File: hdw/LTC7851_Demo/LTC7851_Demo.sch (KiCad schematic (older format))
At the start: 0 parts

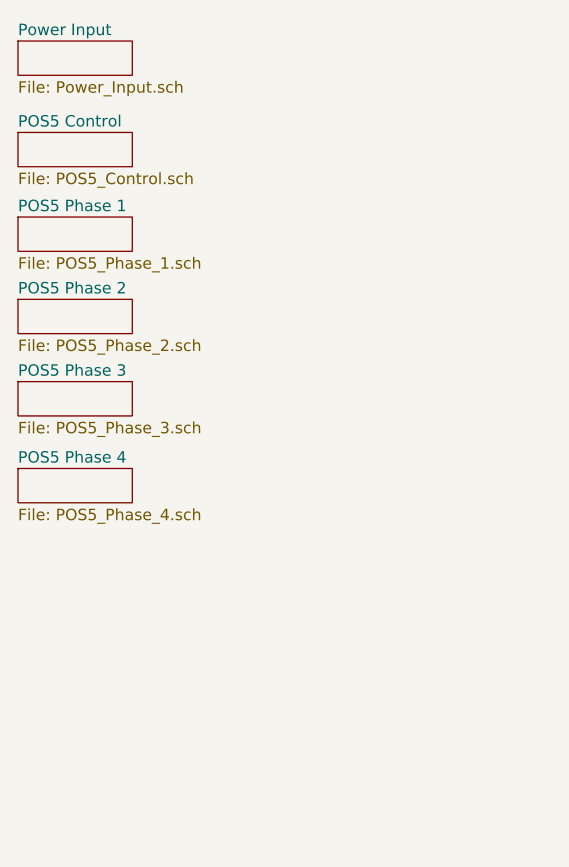
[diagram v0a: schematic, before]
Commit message: Added LDO for VCC input, cleaned some stuff up
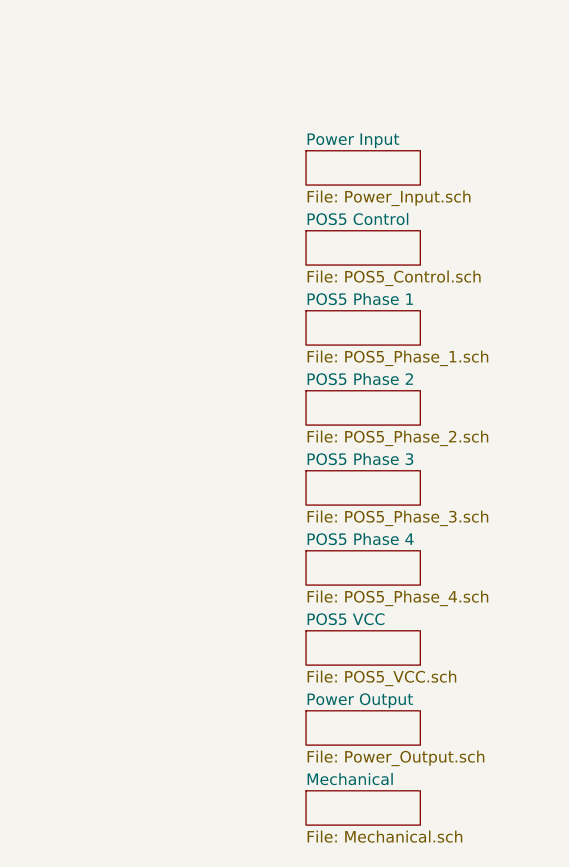
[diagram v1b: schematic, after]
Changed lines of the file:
@@
 $Descr A 11000 8500
 encoding utf-8
-Sheet 1 7
+Sheet 1 10
 Title ""
 Date ""
@@
 $EndDescr
 $Sheet
-S 2010 1500 500  150
+S 3270 1980 500  150
 U 5BB86F23
 F0 "Power Input" 50
@@
 $EndSheet
 $Sheet
-S 2010 1900 500  150
+S 3270 2330 500  150
 U 5BB86F26
 F0 "POS5 Control" 50
@@
 $EndSheet
 $Sheet
-S 2010 2270 500  150
+S 3270 2680 500  150
 U 5BB86F29
 F0 "POS5 Phase 1" 50
@@
 $EndSheet
 $Sheet
-S 2010 2630 500  150
+S 3270 3030 500  150
 U 5BB86F2C
 F0 "POS5 Phase 2" 50
@@
 $EndSheet
 $Sheet
-S 2010 2990 500  150
+S 3270 3380 500  150
 U 5BB86F2F
 F0 "POS5 Phase 3" 50
@@
 $EndSheet
 $Sheet
-S 2010 3370 500  150
+S 3270 3730 500  150
 U 5BB86F32
 F0 "POS5 Phase 4" 50
 F1 "POS5_Phase_4.sch" 50
 $EndSheet
+$Sheet
+S 3270 4080 500  150
+U 5BB9CE4B
+F0 "POS5 VCC" 50
+F1 "POS5_VCC.sch" 50
+$EndSheet
+$Sheet
+S 3270 4430 500  150
+U 5BB9D026
+F0 "Power Output" 50
+F1 "Power_Output.sch" 50
+$EndSheet
+$Sheet
+S 3270 4780 500  150
+U 5BB9D688
+F0 "Mechanical" 50
+F1 "Mechanical.sch" 50
+$EndSheet
 $EndSCHEMATC
